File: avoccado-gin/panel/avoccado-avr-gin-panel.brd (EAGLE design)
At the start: 27 x 14.5 mm, 57 parts, among them Q1 16MHz, Q2 N-FET, U1 MPU-6000QFN-24, U2 MCP73831

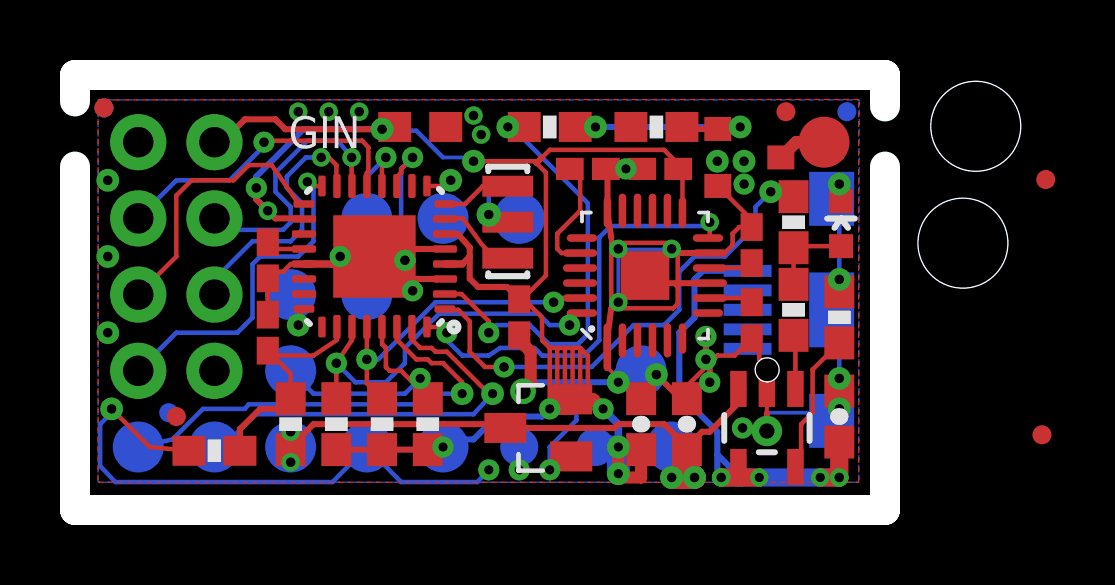
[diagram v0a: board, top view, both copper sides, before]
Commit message: Felina: remove screw mounts, Gin: prepare to panelize
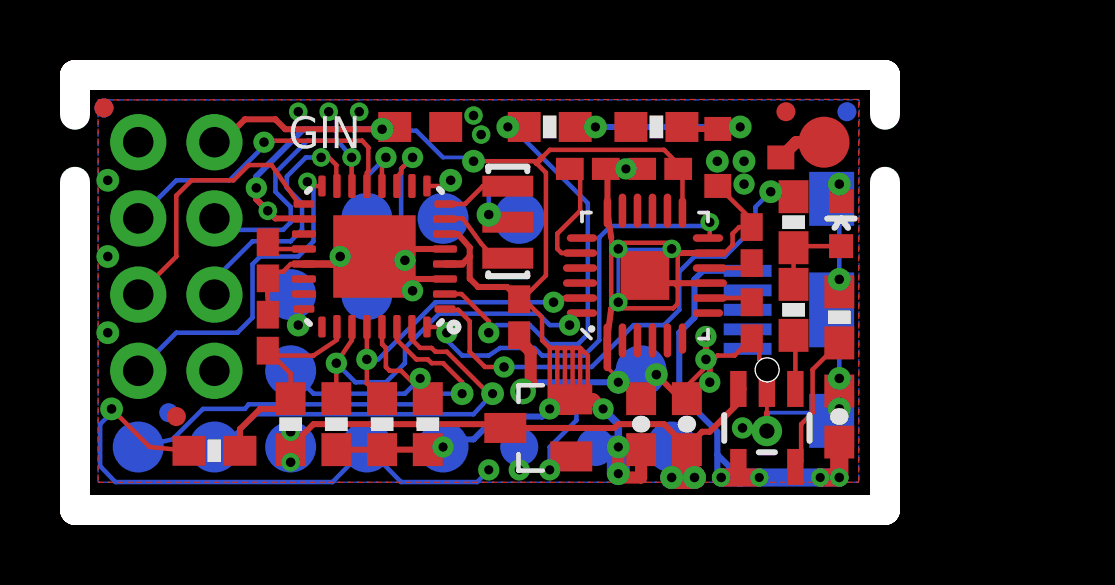
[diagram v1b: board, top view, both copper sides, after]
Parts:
- removed FID1, FID3: FIDUCIALUFIDUCIAL, SparkFun-Aesthetics:MICRO-FIDUCIAL
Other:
- outline, holes or cut-outs redrawn
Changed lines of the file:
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@@
 <setting verticaltext="up"/>
 </settings>
-<grid distance="0.02" unitdist="inch" unit="inch" style="lines" multiple="1" display="yes" altdistance="0.01" altunitdist="inch" altunit="inch"/>
+<grid distance="1" unitdist="mm" unit="mm" style="lines" multiple="1" display="yes" altdistance="0.1" altunitdist="mm" altunit="mm"/>
 <layers>
 <layer number="1" name="Top" color="47" fill="1" visible="yes" active="yes"/>
@@
 <text x="20.83149375" y="3.812428125" size="1.778" layer="22" font="vector" ratio="15" rot="MR0" align="top-left">+</text>
 <text x="9.0296" y="11.5856" size="1.0668" layer="21" ratio="15" rot="R180" align="top-left">GIN</text>
-<wire x1="-0.4824" y1="10.9756" x2="-0.4824" y2="-0.4744" width="1" layer="46"/>
+<wire x1="-0.4824" y1="10.4676" x2="-0.4824" y2="-0.4744" width="1" layer="46"/>
 <wire x1="-0.4824" y1="-0.4744" x2="26.5176" y2="-0.4744" width="1" layer="46"/>
-<wire x1="26.5176" y1="-0.4744" x2="26.5176" y2="10.9756" width="1" layer="46"/>
+<wire x1="26.5176" y1="-0.4744" x2="26.5176" y2="10.4676" width="1" layer="46"/>
 <rectangle x1="7.4676" y1="5.9436" x2="11.5316" y2="10.0076" layer="41"/>
 <circle x="0.4826" y="12.9286" radius="0.254" width="0.6096" layer="29"/>
-<circle x="31.75" y="2.032" radius="0.254" width="0.6096" layer="29"/>
-<circle x="31.877" y="10.541" radius="0.254" width="0.6096" layer="29"/>
-<hole x="29.115" y="8.42" drill="3"/>
-<hole x="29.543" y="12.316" drill="3"/>
-<wire x1="26.5176" y1="12.9756" x2="26.5176" y2="14.0256" width="1" layer="46"/>
+<wire x1="26.5176" y1="12.7" x2="26.5176" y2="14.0256" width="1" layer="46"/>
 <wire x1="26.5176" y1="14.0256" x2="-0.4824" y2="14.0256" width="1" layer="46"/>
-<wire x1="-0.4824" y1="14.0256" x2="-0.4824" y2="13.1436" width="1" layer="46"/>
+<wire x1="-0.4824" y1="14.0256" x2="-0.4824" y2="12.7" width="1" layer="46"/>
 <wire x1="1.3716" y1="2.3876" x2="0.6096" y2="0.6096" width="0.1778" layer="29"/>
 <wire x1="1.3716" y1="2.3876" x2="2.1336" y2="0.6096" width="0.1778" layer="29"/>
@@
 </element>
 <element name="FID2" library="SparkFun-Aesthetics" package="MICRO-FIDUCIAL" value="FIDUCIALUFIDUCIAL" x="0.4826" y="12.9286"/>
-<element name="FID1" library="SparkFun-Aesthetics" package="MICRO-FIDUCIAL" value="FIDUCIALUFIDUCIAL" x="31.877" y="10.541"/>
-<element name="FID3" library="SparkFun-Aesthetics" package="MICRO-FIDUCIAL" value="FIDUCIALUFIDUCIAL" x="31.75" y="2.032"/>
 <element name="JP22" library="SparkFun-Connectors" package="USB-B-MICRO-SMD_V03" value="USB_MICROB_PLUGCONN-11752" x="24.7396" y="6.1976" smashed="yes" rot="MR0">
 <attribute name="PROD_ID" value="CONN-11752" x="24.7396" y="6.1976" size="1.778" layer="28" font="vector" ratio="15" rot="MR0" display="off"/>
